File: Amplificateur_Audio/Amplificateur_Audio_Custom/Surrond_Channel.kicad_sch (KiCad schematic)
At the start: 84 parts, among them J401 SL+, J402 SL-, J403 SR+, J404 SR-, J405 Analog input Connector, U401 PCM5252RHBR, U402 TPA3244DDWR, U403 74LVC1G125, U404 74LVC1G125

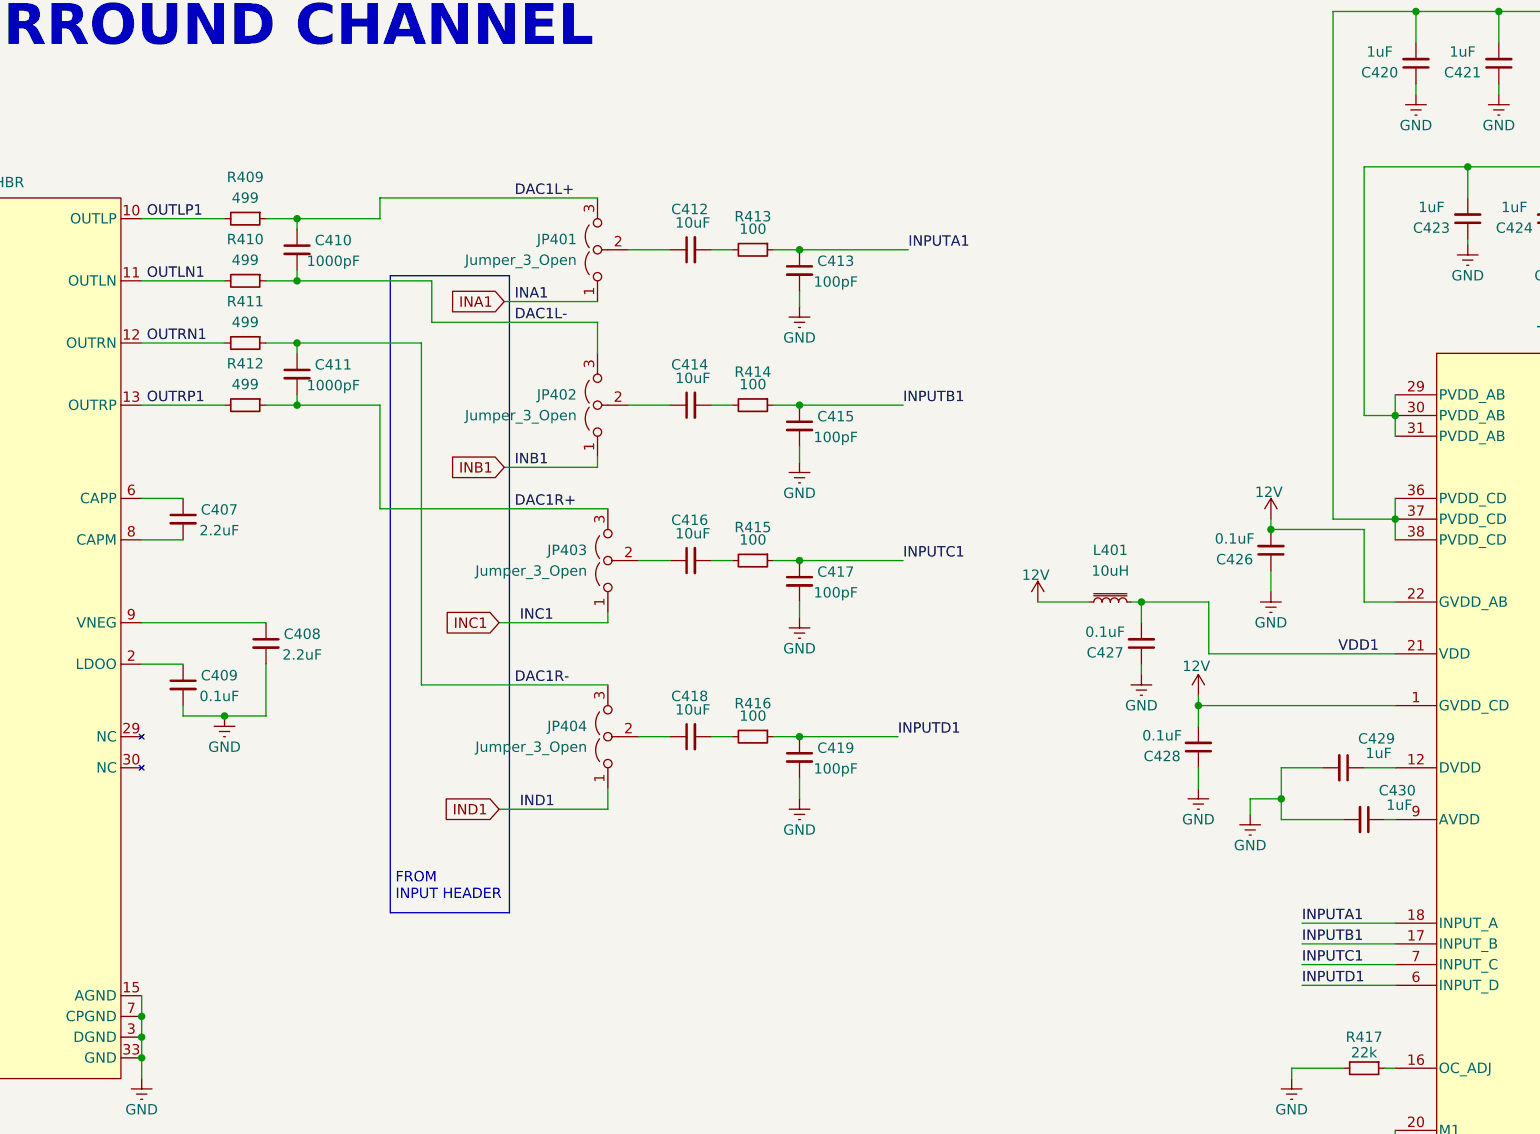
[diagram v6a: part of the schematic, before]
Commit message: Routage symétrique
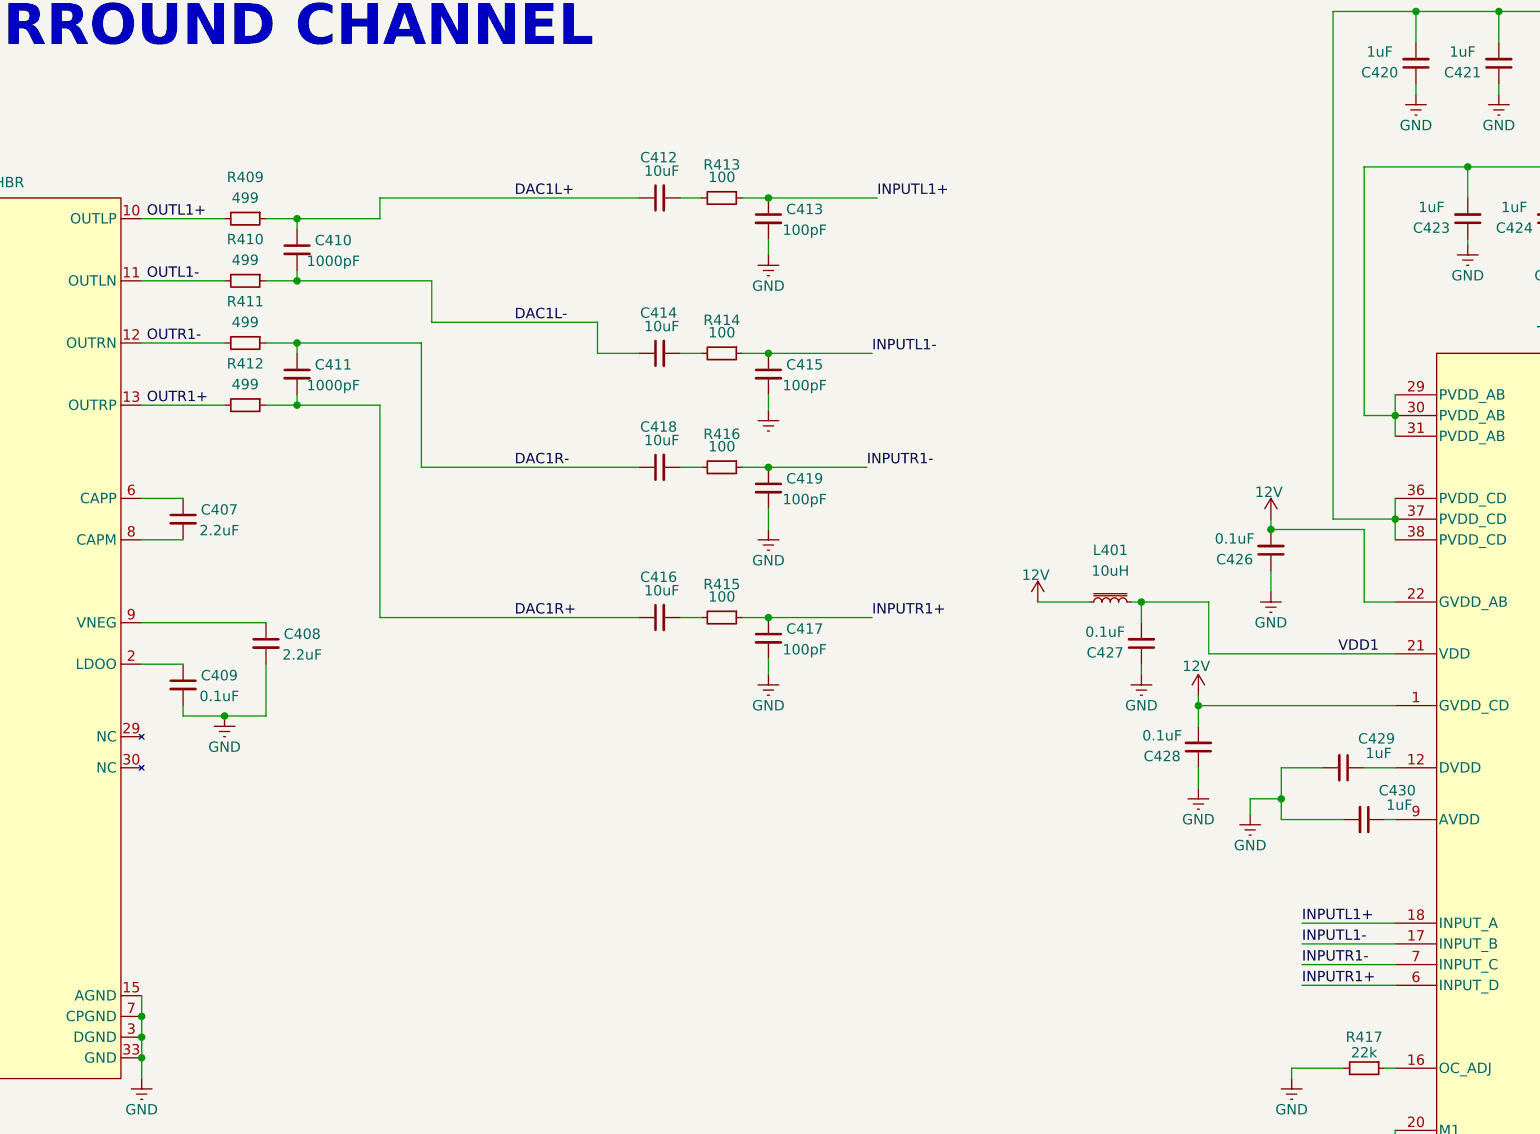
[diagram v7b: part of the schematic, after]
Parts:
- removed JP401, JP402, JP403, JP404: Jumper_3_Open, Connector_PinHeader_2.54mm:PinHeader_1x03_P2.54mm_Vertical_SMD_Pin1Left, symbol Jumper:Jumper_3_Open
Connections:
- net DAC1L+: now also C412.1
- net DAC1L-: now also C414.1
- net DAC1R+: now also C416.1
- net DAC1R-: now also C418.1
- net INPUTA1 renamed INPUTL1+
- net INPUTB1 renamed INPUTL1-
- net INPUTC1 renamed INPUTR1+
- net INPUTR1+: now also U402.6 (INPUT_D); no longer U402.7 (INPUT_C)
- net INPUTD1 renamed INPUTR1-
- net INPUTR1-: now also U402.7 (INPUT_C); no longer U402.6 (INPUT_D)
- net OUTLN1 renamed OUTL1-
- net OUTLP1 renamed OUTL1+
- net OUTRN1 renamed OUTR1-
- net OUTRP1 renamed OUTR1+
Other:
- note removed: "FROM INPUT HEADER"
- moved on the sheet: C412, C413, C414, C415, C416, C417, C418, C419, R413, R414, R415, R416

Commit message: Amélioration du routage
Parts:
- C401, C403, C405, C413, C415, C417, C419, C426, C427, C428, C429, C430, C431, C446: footprint Capacitor_SMD:C_0603_1608Metric_Pad1.08x0.95mm_HandSolder -> Capacitor_SMD:C_0603_1608Metric
- C402, C404, C406, C407, C408, C409: footprint Capacitor_SMD:C_0402_1005Metric_Pad0.74x0.62mm_HandSolder -> Capacitor_SMD:C_0402_1005Metric
- C412, C414, C416, C418: footprint Capacitor_SMD:C_1206_3216Metric_Pad1.33x1.80mm_HandSolder -> Capacitor_SMD:C_1206_3216Metric
- L401: footprint Inductor_SMD:L_0603_1608Metric_Pad1.05x0.95mm_HandSolder -> Inductor_SMD:L_0603_1608Metric
- R401, R402, R403, R404, R405, R406, R407: footprint Resistor_SMD:R_0402_1005Metric_Pad0.72x0.64mm_HandSolder -> Resistor_SMD:R_0402_1005Metric
- R408, R413, R414, R415, R416, R417, R418: footprint Resistor_SMD:R_0603_1608Metric_Pad0.98x0.95mm_HandSolder -> Resistor_SMD:R_0603_1608Metric
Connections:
- net AVDD: now reaches C404.2, C405.2, R408.1, U401.14 (AVDD)
- net DACF1L+: now reaches C412.2, R413.2
- net DACF1R+: now reaches C416.2, R415.2
- net DACF1R-: now reaches C418.2, R416.2
- net DACF1L-: now reaches C414.2, R414.2
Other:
- moved on the sheet: C412, C414, C416, C418
